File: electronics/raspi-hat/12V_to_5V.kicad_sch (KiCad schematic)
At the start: 6 parts, among them U5 MYMGA5R04RELA5RA

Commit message: Start laying out PCB for raspberry pi hat
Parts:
- C7, C8: footprint (none) -> Capacitor_SMD:C_0603_1608Metric
- R7, R8, R9: footprint (none) -> Resistor_SMD:R_0603_1608Metric
- U5: footprint MYMGA5R04RELA5RA_MUR -> MYMGA5R04RELA5RA:MYMGA5R04RELA5RA

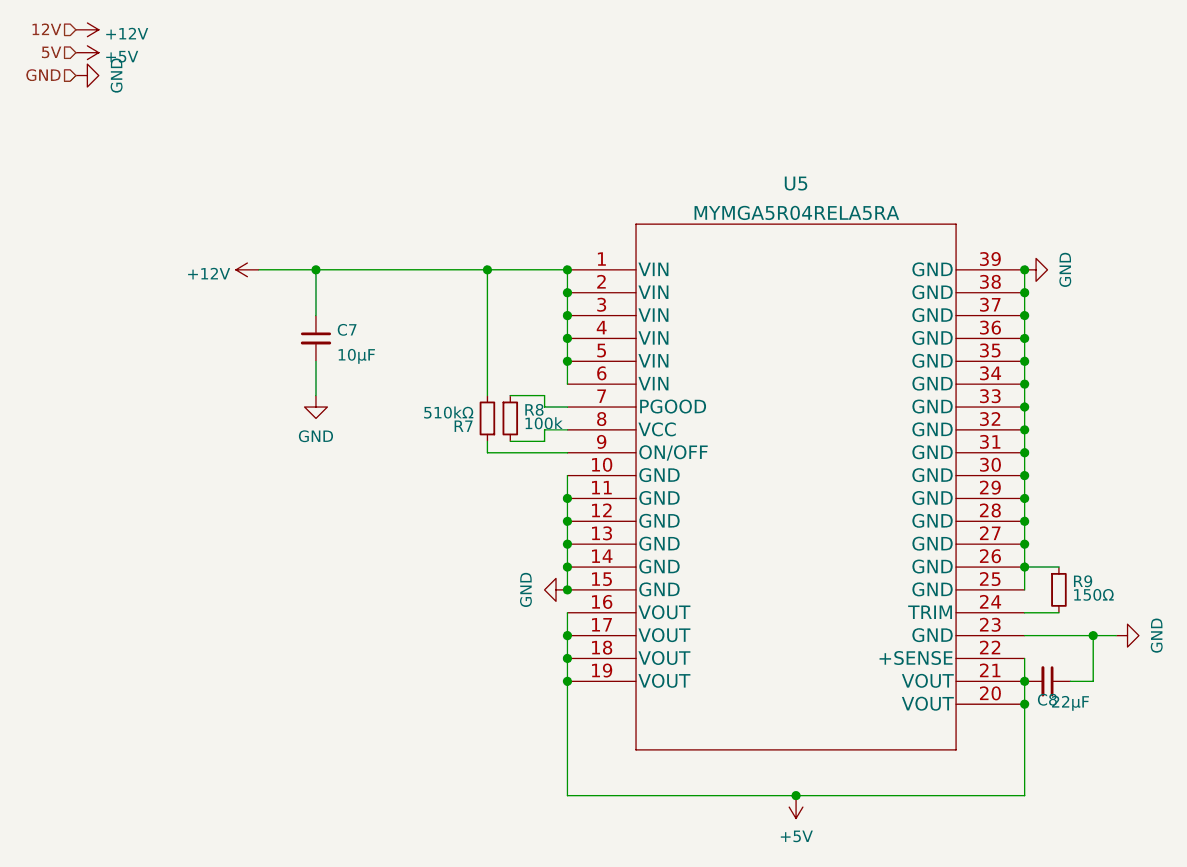
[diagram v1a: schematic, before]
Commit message: Finish designing raspi hat
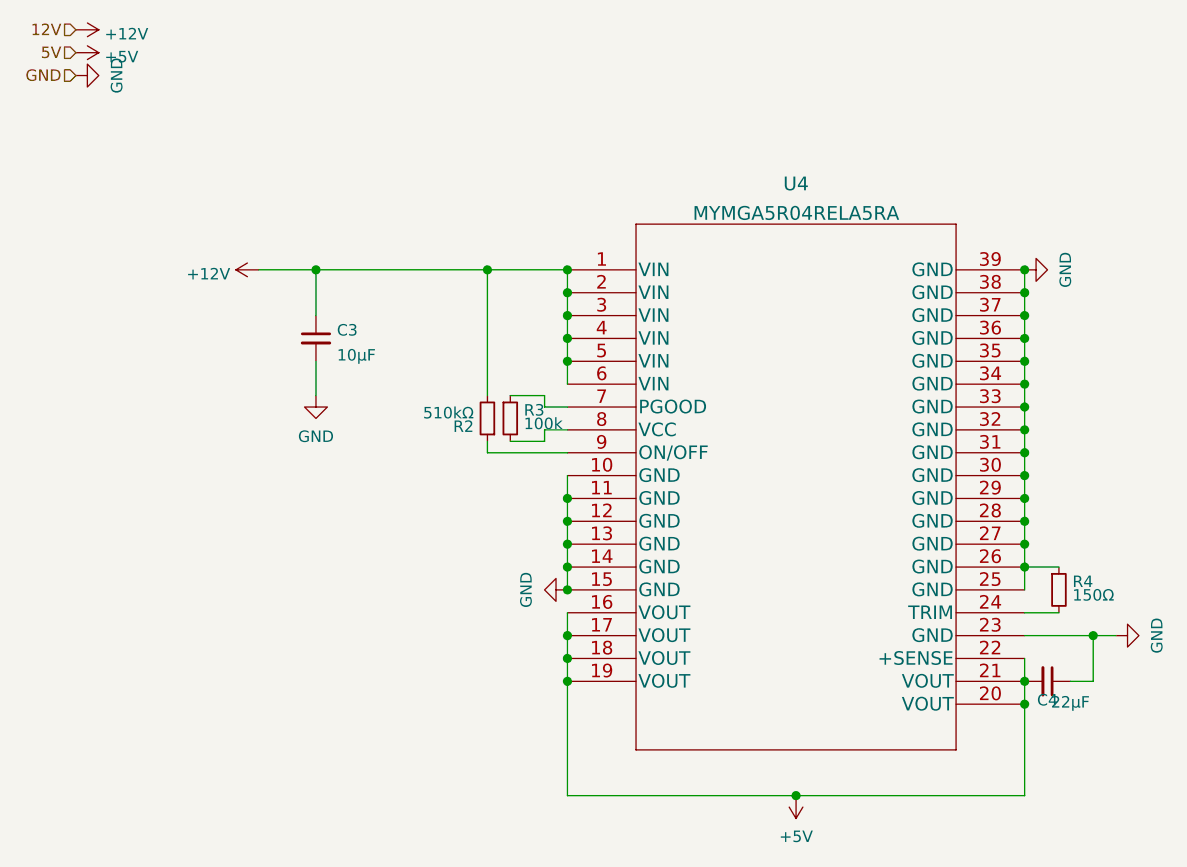
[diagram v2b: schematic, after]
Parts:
- renumbered C7 to C3, C8 to C4, R7 to R2, R8 to R3, R9 to R4, U5 to U4
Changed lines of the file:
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@@
   (symbol (lib_id "MYMGA5R04RELA5RA:MYMGA5R04RELA5RA") (at 74.93 52.07 0) (unit 1)
     (in_bom yes) (on_board yes) (fields_autoplaced)
-    (property "Reference" "U5" (id 0) (at 100.33 42.5225 0)
+    (property "Reference" "U4" (id 0) (at 100.33 42.5225 0)
       (effects (font (size 1.524 1.524)))
     )
@@
   (symbol (lib_id "power:GND") (at 125.73 52.07 90) (unit 1)
     (in_bom yes) (on_board yes)
-    (property "Reference" "#PWR0115" (id 0) (at 132.08 52.07 0)
+    (property "Reference" "#PWR0117" (id 0) (at 132.08 52.07 0)
       (effects (font (size 1.27 1.27)) hide)
     )
@@
   (symbol (lib_id "Device:C_Small") (at 46.99 59.69 0) (unit 1)
     (in_bom yes) (on_board yes) (fields_autoplaced)
-    (property "Reference" "C7" (id 0) (at 49.3142 58.7815 0)
+    (property "Reference" "C3" (id 0) (at 49.3142 58.7815 0)
       (effects (font (size 1.27 1.27)) (justify left))
     )
@@
   (symbol (lib_id "Device:C_Small") (at 128.27 97.79 270) (unit 1)
     (in_bom yes) (on_board yes)
-    (property "Reference" "C8" (id 0) (at 128.27 99.8813 90))
+    (property "Reference" "C4" (id 0) (at 128.27 99.8813 90))
     (property "Value" "22μF" (id 1) (at 130.81 100.1164 90))
     (property "Footprint" "Capacitor_SMD:C_0603_1608Metric" (id 2) (at 128.27 97.79 0)
@@
   (symbol (lib_id "power:GND") (at 74.93 87.63 270) (unit 1)
     (in_bom yes) (on_board yes)
-    (property "Reference" "#PWR0116" (id 0) (at 68.58 87.63 0)
+    (property "Reference" "#PWR0111" (id 0) (at 68.58 87.63 0)
       (effects (font (size 1.27 1.27)) hide)
     )
@@
   (symbol (lib_id "Device:R_Small") (at 68.58 68.58 0) (unit 1)
     (in_bom yes) (on_board yes)
-    (property "Reference" "R8" (id 0) (at 70.0787 67.6715 0)
+    (property "Reference" "R3" (id 0) (at 70.0787 67.6715 0)
       (effects (font (size 1.27 1.27)) (justify left))
     )
@@
   (symbol (lib_id "power:GND") (at 20.32 30.48 90) (unit 1)
     (in_bom yes) (on_board yes)
-    (property "Reference" "#PWR0119" (id 0) (at 26.67 30.48 0)
+    (property "Reference" "#PWR0114" (id 0) (at 26.67 30.48 0)
       (effects (font (size 1.27 1.27)) hide)
     )
@@
   (symbol (lib_id "power:+5V") (at 20.32 27.94 270) (unit 1)
     (in_bom yes) (on_board yes) (fields_autoplaced)
-    (property "Reference" "#PWR0118" (id 0) (at 16.51 27.94 0)
+    (property "Reference" "#PWR0112" (id 0) (at 16.51 27.94 0)
       (effects (font (size 1.27 1.27)) hide)
     )
@@
   (symbol (lib_id "Device:R_Small") (at 66.04 68.58 180) (unit 1)
     (in_bom yes) (on_board yes)
-    (property "Reference" "R7" (id 0) (at 64.5413 69.4885 0)
+    (property "Reference" "R2" (id 0) (at 64.5413 69.4885 0)
       (effects (font (size 1.27 1.27)) (justify left))
     )
@@
   (symbol (lib_id "power:GND") (at 135.89 92.71 90) (unit 1)
     (in_bom yes) (on_board yes)
-    (property "Reference" "#PWR0123" (id 0) (at 142.24 92.71 0)
+    (property "Reference" "#PWR0116" (id 0) (at 142.24 92.71 0)
       (effects (font (size 1.27 1.27)) hide)
     )
@@
   (symbol (lib_id "power:GND") (at 46.99 66.04 0) (unit 1)
     (in_bom yes) (on_board yes)
-    (property "Reference" "#PWR0120" (id 0) (at 46.99 72.39 0)
+    (property "Reference" "#PWR0110" (id 0) (at 46.99 72.39 0)
       (effects (font (size 1.27 1.27)) hide)
     )
@@
   (symbol (lib_id "power:+12V") (at 20.32 25.4 270) (unit 1)
     (in_bom yes) (on_board yes) (fields_autoplaced)
-    (property "Reference" "#PWR0117" (id 0) (at 16.51 25.4 0)
+    (property "Reference" "#PWR0113" (id 0) (at 16.51 25.4 0)
       (effects (font (size 1.27 1.27)) hide)
     )
@@
   (symbol (lib_id "Device:R_Small") (at 129.54 87.63 0) (unit 1)
     (in_bom yes) (on_board yes)
-    (property "Reference" "R9" (id 0) (at 131.0387 86.7215 0)
+    (property "Reference" "R4" (id 0) (at 131.0387 86.7215 0)
       (effects (font (size 1.27 1.27)) (justify left))
     )
@@
   (symbol (lib_id "power:+12V") (at 40.64 52.07 90) (unit 1)
     (in_bom yes) (on_board yes) (fields_autoplaced)
-    (property "Reference" "#PWR0121" (id 0) (at 44.45 52.07 0)
+    (property "Reference" "#PWR0115" (id 0) (at 44.45 52.07 0)
       (effects (font (size 1.27 1.27)) hide)
     )
@@
   (symbol (lib_id "power:+5V") (at 100.33 110.49 180) (unit 1)
     (in_bom yes) (on_board yes) (fields_autoplaced)
-    (property "Reference" "#PWR0122" (id 0) (at 100.33 106.68 0)
-      (effects (font (size 1.27 1.27)) hide)
-    )
+    (property "Reference" "#PWR0109" (id 0) (at 100.33 106.68 0)
+      (effects (font (size 1.27 1.27)) hide)
+    )
